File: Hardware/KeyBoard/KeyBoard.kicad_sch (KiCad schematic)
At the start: 0 parts

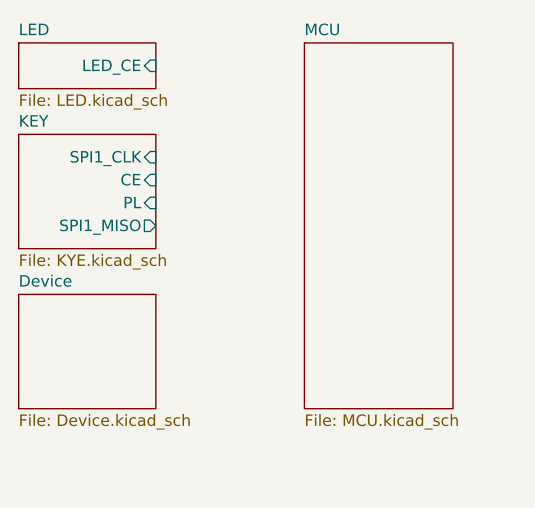
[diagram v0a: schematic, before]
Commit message: Completed the schematic drawing, started the PCB process, and updated the firmware to the helloword firmware.
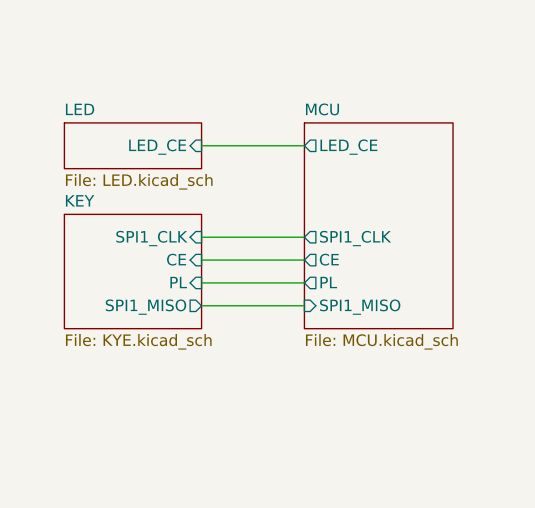
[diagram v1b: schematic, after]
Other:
- removed sheet Device
- sheet MCU ports: added CE, LED_CE, PL, SPI1_CLK, SPI1_MISO; removed none
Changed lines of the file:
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@@
 	(generator_version "8.0")
 	(paper "A4")
+	(wire
+		(pts
+			(xy 63.5 57.15) (xy 74.93 57.15)
+		)
+		(stroke
+			(width 0)
+			(type default)
+		)
+	)
+	(wire
+		(pts
+			(xy 63.5 46.99) (xy 74.93 46.99)
+		)
+		(stroke
+			(width 0)
+			(type default)
+		)
+	)
+	(wire
+		(pts
+			(xy 63.5 62.23) (xy 74.93 62.23)
+		)
+		(stroke
+			(width 0)
+			(type default)
+		)
+	)
+	(wire
+		(pts
+			(xy 63.5 64.77) (xy 74.93 64.77)
+		)
+		(stroke
+			(width 0)
+			(type default)
+		)
+	)
+	(wire
+		(pts
+			(xy 63.5 59.69) (xy 74.93 59.69)
+		)
+		(stroke
+			(width 0)
+			(type default)
+		)
+	)
 	(sheet
-		(at 43.18 45.72)
+		(at 48.26 54.61)
 		(size 15.24 12.7)
 		(fields_autoplaced yes)
@@
 		)
 		(property "Sheetname" "KEY"
-			(at 43.18 45.0084 0)
+			(at 48.26 53.8984 0)
 			(effects
 				(font
@@
 		)
 		(property "Sheetfile" "KYE.kicad_sch"
-			(at 43.18 59.0046 0)
+			(at 48.26 67.8946 0)
 			(effects
 				(font
@@
 		)
 		(pin "SPI1_CLK" input
-			(at 58.42 48.26 0)
+			(at 63.5 57.15 0)
 			(effects
 				(font
@@
 		)
 		(pin "CE" input
-			(at 58.42 50.8 0)
+			(at 63.5 59.69 0)
 			(effects
 				(font
@@
 		)
 		(pin "PL" input
-			(at 58.42 53.34 0)
+			(at 63.5 62.23 0)
 			(effects
 				(font
@@
 		)
 		(pin "SPI1_MISO" output
-			(at 58.42 55.88 0)
+			(at 63.5 64.77 0)
 			(effects
 				(font
@@
 	)
 	(sheet
-		(at 74.93 35.56)
-		(size 16.51 40.64)
+		(at 74.93 44.45)
+		(size 16.51 22.86)
 		(fields_autoplaced yes)
 		(stroke
@@
 		)
 		(property "Sheetname" "MCU"
-			(at 74.93 34.8484 0)
+			(at 74.93 43.7384 0)
 			(effects
 				(font
@@
 		)
 		(property "Sheetfile" "MCU.kicad_sch"
-			(at 74.93 76.7846 0)
+			(at 74.93 67.8946 0)
 			(effects
 				(font
@@
 				)
 				(justify left top)
+			)
+		)
+		(pin "SPI1_MISO" input
+			(at 74.93 64.77 180)
+			(effects
+				(font
+					(size 1.27 1.27)
+				)
+				(justify left)
+			)
+		)
+		(pin "SPI1_CLK" output
+			(at 74.93 57.15 180)
+			(effects
+				(font
+					(size 1.27 1.27)
+				)
+				(justify left)
+			)
+		)
+		(pin "LED_CE" output
+			(at 74.93 46.99 180)
+			(effects
+				(font
+					(size 1.27 1.27)
+				)
+				(justify left)
+			)
+		)
+		(pin "CE" output
+			(at 74.93 59.69 180)
+			(effects
+				(font
+					(size 1.27 1.27)
+				)
+				(justify left)
+			)
+		)
+		(pin "PL" output
+			(at 74.93 62.23 180)
+			(effects
+				(font
+					(size 1.27 1.27)
+				)
+				(justify left)
 			)
 		)
@@
 	)
 	(sheet
-		(at 43.18 63.5)
-		(size 15.24 12.7)
+		(at 48.26 44.45)
+		(size 15.24 5.08)
 		(fields_autoplaced yes)
 		(stroke
@@
 			(color 255 255 255 1.0000)
 		)
-		(property "Sheetname" "Device"
-			(at 43.18 62.7884 0)
+		(property "Sheetname" "LED"
+			(at 48.26 43.7384 0)
 			(effects
 				(font
@@
 			)
 		)
-		(property "Sheetfile" "Device.kicad_sch"
-			(at 43.18 76.7846 0)
+		(property "Sheetfile" "LED.kicad_sch"
+			(at 48.26 50.1146 0)
 			(effects
 				(font
@@
 			)
 		)
-		(instances
-			(project "KeyBoard"
-				(path "/241a990a-4472-4769-ab02-cee073c97173"
-					(page "5")
-				)
-			)
-		)
-	)
-	(sheet
-		(at 43.18 35.56)
-		(size 15.24 5.08)
-		(fields_autoplaced yes)
-		(stroke
-			(width 0.1524)
-			(type solid)
-			(color 52 0 255 1)
-		)
-		(fill
-			(color 255 255 255 1.0000)
-		)
-		(property "Sheetname" "LED"
-			(at 43.18 34.8484 0)
-			(effects
-				(font
-					(size 1.27 1.27)
-				)
-				(justify left bottom)
-			)
-		)
-		(property "Sheetfile" "LED.kicad_sch"
-			(at 43.18 41.2246 0)
-			(effects
-				(font
-					(size 1.27 1.27)
-				)
-				(justify left top)
-			)
-		)
 		(pin "LED_CE" input
-			(at 58.42 38.1 0)
-			(effects
-				(font
+			(at 63.5 46.99 0)
+			(effects
+				(font

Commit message: complete layout
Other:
- added sheet Device (Device.kicad_sch)
- sheet MCU ports: added UART_RX, UART_TX, USB_PORT_N, USB_PORT_P; removed none
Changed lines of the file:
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@@
+	(wire
+		(pts
+			(xy 63.5 73.66) (xy 74.93 73.66)
+		)
+		(stroke
+			(width 0)
+			(type default)
+		)
+	)
+	(wire
+		(pts
+			(xy 63.5 80.01) (xy 74.93 80.01)
+		)
+		(stroke
+			(width 0)
+			(type default)
+		)
+	)
 	(wire
 		(pts
@@
 		(pts
 			(xy 63.5 59.69) (xy 74.93 59.69)
+		)
+		(stroke
+			(width 0)
+			(type default)
+		)
+	)
+	(wire
+		(pts
+			(xy 63.5 74.93) (xy 74.93 74.93)
+		)
+		(stroke
+			(width 0)
+			(type default)
+		)
+	)
+	(wire
+		(pts
+			(xy 63.5 78.74) (xy 74.93 78.74)
 		)
 		(stroke
@@
 	(sheet
 		(at 74.93 44.45)
-		(size 16.51 22.86)
+		(size 16.51 38.1)
 		(fields_autoplaced yes)
 		(stroke
@@
 		)
 		(property "Sheetfile" "MCU.kicad_sch"
-			(at 74.93 67.8946 0)
+			(at 74.93 83.1346 0)
 			(effects
 				(font
@@
 		(pin "PL" output
 			(at 74.93 62.23 180)
+			(effects
+				(font
+					(size 1.27 1.27)
+				)
+				(justify left)
+			)
+		)
+		(pin "USB_PORT_P" bidirectional
+			(at 74.93 73.66 180)
+			(effects
+				(font
+					(size 1.27 1.27)
+				)
+				(justify left)
+			)
+		)
+		(pin "USB_PORT_N" bidirectional
+			(at 74.93 74.93 180)
+			(effects
+				(font
+					(size 1.27 1.27)
+				)
+				(justify left)
+			)
+		)
+		(pin "UART_RX" input
+			(at 74.93 78.74 180)
+			(effects
+				(font
+					(size 1.27 1.27)
+				)
+				(justify left)
+			)
+		)
+		(pin "UART_TX" output
+			(at 74.93 80.01 180)
 			(effects
 				(font
@@
 				)
 			)
+		)
+	)
+	(sheet
+		(at 48.26 72.39)
+		(size 15.24 10.16)
+		(fields_autoplaced yes)
+		(stroke
+			(width 0.1524)
+			(type solid)
+			(color 52 0 255 1)
+		)
+		(fill
+			(color 255 255 255 1.0000)
+		)
+		(property "Sheetname" "Device"
+			(at 48.26 71.6784 0)
+			(effects
+				(font
+					(size 1.27 1.27)
+				)
+				(justify left bottom)
+			)
+		)
+		(property "Sheetfile" "Device.kicad_sch"
+			(at 48.26 83.1346 0)
+			(effects
+				(font
+					(size 1.27 1.27)
+				)
+				(justify left top)
+			)
+		)
+		(pin "USB_DM_1" bidirectional
+			(at 63.5 74.93 0)
+			(effects
+				(font
+					(size 1.27 1.27)
+				)
+				(justify right)
+			)
+		)
+		(pin "USB_DP_1" bidirectional
+			(at 63.5 73.66 0)
+			(effects
+				(font
+					(size 1.27 1.27)
+				)
+				(justify right)
+			)
+		)
+		(pin "UART_RX" output
+			(at 63.5 78.74 0)
+			(effects
+				(font
+					(size 1.27 1.27)
+				)
+				(justify right)
+			)
+		)
+		(pin "UART_TX" input
+			(at 63.5 80.01 0)
+			(effects
+				(font
+					(size 1.27 1.27)
+				)
+				(justify right)
+			)
+		)
+		(instances
+			(project "KeyBoard"
+				(path "/241a990a-4472-4769-ab02-cee073c97173"
+					(page "5")
+				)
+			)

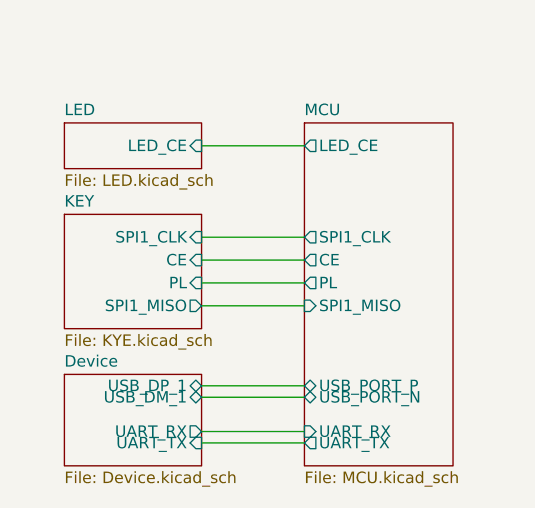
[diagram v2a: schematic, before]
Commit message: Update the PCB layout
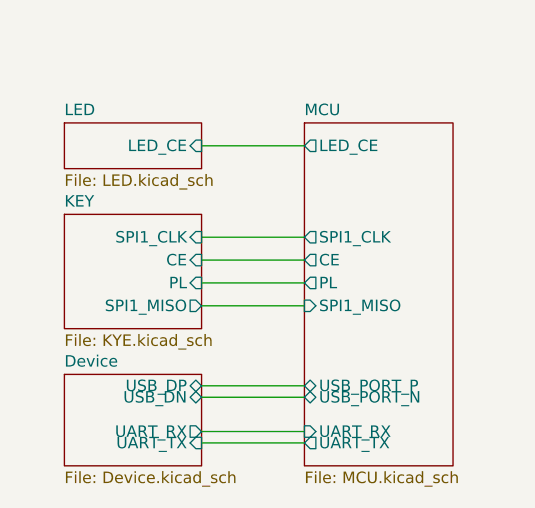
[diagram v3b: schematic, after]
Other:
- sheet Device ports: added USB_DN, USB_DP; removed USB_DM_1, USB_DP_1
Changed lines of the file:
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@@
+	(wire
+		(pts
+			(xy 63.5 80.01) (xy 74.93 80.01)
+		)
+		(stroke
+			(width 0)
+			(type default)
+		)
+	)
+	(wire
+		(pts
+			(xy 63.5 57.15) (xy 74.93 57.15)
+		)
+		(stroke
+			(width 0)
+			(type default)
+		)
+	)
 	(wire
 		(pts
 			(xy 63.5 73.66) (xy 74.93 73.66)
-		)
-		(stroke
-			(width 0)
-			(type default)
-		)
-	)
-	(wire
-		(pts
-			(xy 63.5 80.01) (xy 74.93 80.01)
-		)
-		(stroke
-			(width 0)
-			(type default)
-		)
-	)
-	(wire
-		(pts
-			(xy 63.5 57.15) (xy 74.93 57.15)
 		)
 		(stroke
@@
 			)
 		)
-		(pin "USB_DM_1" bidirectional
-			(at 63.5 74.93 0)
-			(effects
-				(font
-					(size 1.27 1.27)
-				)
-				(justify right)
-			)
-		)
-		(pin "USB_DP_1" bidirectional
-			(at 63.5 73.66 0)
-			(effects
-				(font
-					(size 1.27 1.27)
-				)
-				(justify right)
-			)
-		)
 		(pin "UART_RX" output
 			(at 63.5 78.74 0)
@@
 			(effects
 				(font
+					(size 1.27 1.27)
+				)
+				(justify right)
+			)
+		)
+		(pin "USB_DP" bidirectional
+			(at 63.5 73.66 0)
+			(effects
+				(font
+					(size 1.27 1.27)
+				)
+				(justify right)
+			)
+		)
+		(pin "USB_DN" bidirectional
+			(at 63.5 74.93 0)
+			(effects
+				(font
